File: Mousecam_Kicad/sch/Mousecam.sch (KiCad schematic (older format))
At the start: 16 parts

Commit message: sync
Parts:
- removed U?: TLV7103318DSER, DSE6, symbol Mousecam-rescue:TLV7103318DSER-TLV7103318DSER-Mousecam-rescue
- added U?: TLV7103318DSER, DSE6, symbol TLV7103318DSER:TLV7103318DSER
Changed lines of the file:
@@
 Wire Wire Line
 	8250 5350 8250 5550
-$Comp
-L Mousecam-rescue:TLV7103318DSER-TLV7103318DSER-Mousecam-rescue U?
-U 1 1 607F86D1
-P 2800 1400
-F 0 "U?" H 3450 1787 60  0000 C CNN
-F 1 "TLV7103318DSER" H 3450 1681 60  0000 C CNN
-F 2 "DSE6" H 3450 1650 60  0001 C CNN
-F 3 "" H 2800 1400 60  0000 C CNN
-	1    2800 1400
-	1    0    0    -1
-$EndComp
 $Sheet
 S 9750 5300 1700 1500
@@
 F15 "I2C_SCL" I L 9750 6700 50
 $EndSheet
+$Comp
+L TLV7103318DSER:TLV7103318DSER U?
+U 1 1 608A8B14
+P 2800 1400
+F 0 "U?" H 3450 1787 60  0000 C CNN
+F 1 "TLV7103318DSER" H 3450 1681 60  0000 C CNN
+F 2 "DSE6" H 3450 1650 60  0001 C CNN
+F 3 "" H 2800 1400 60  0000 C CNN
+	1    2800 1400
+	1    0    0    -1
+$EndComp
 $EndSCHEMATC

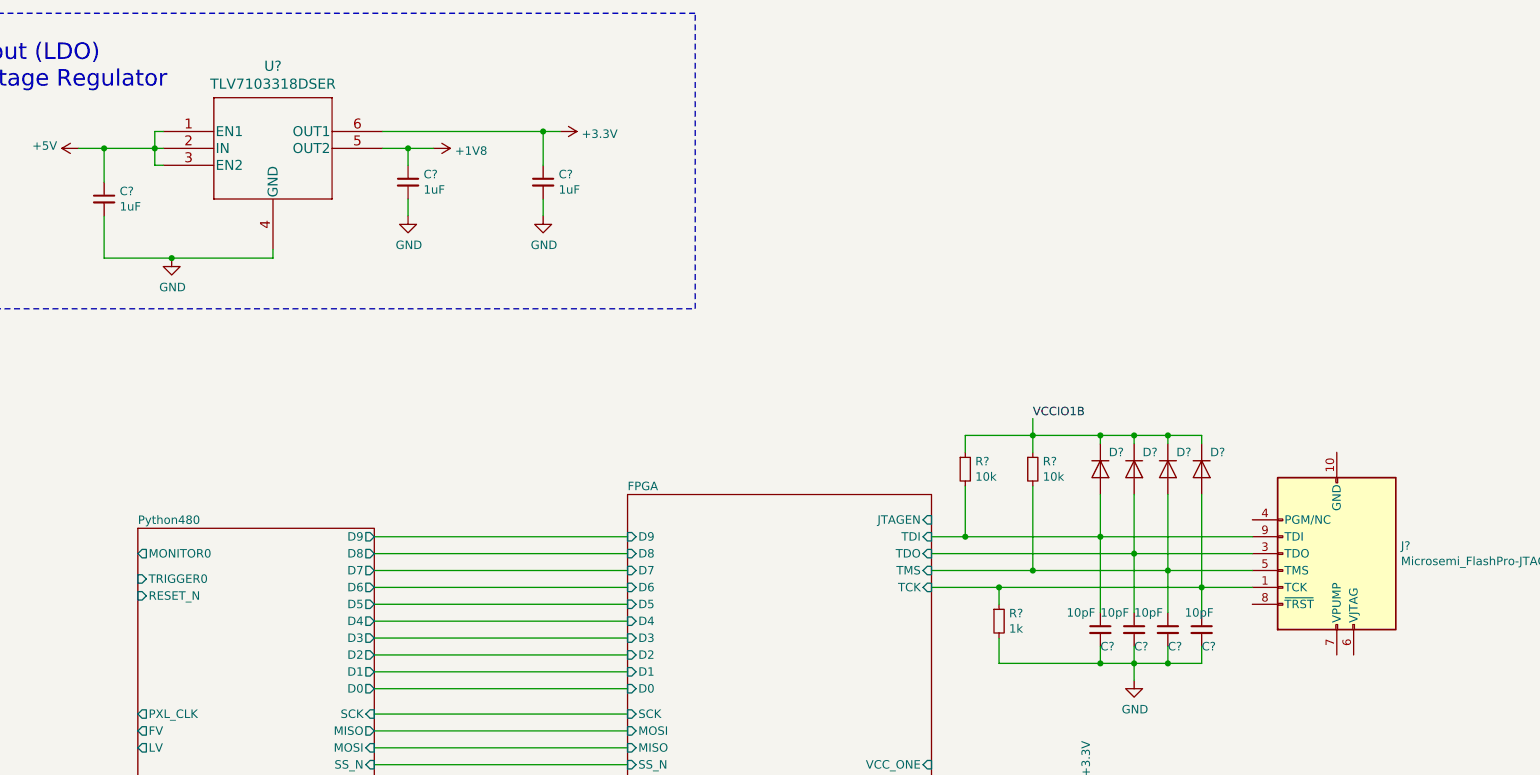
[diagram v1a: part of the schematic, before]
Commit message: updated relative path for libs
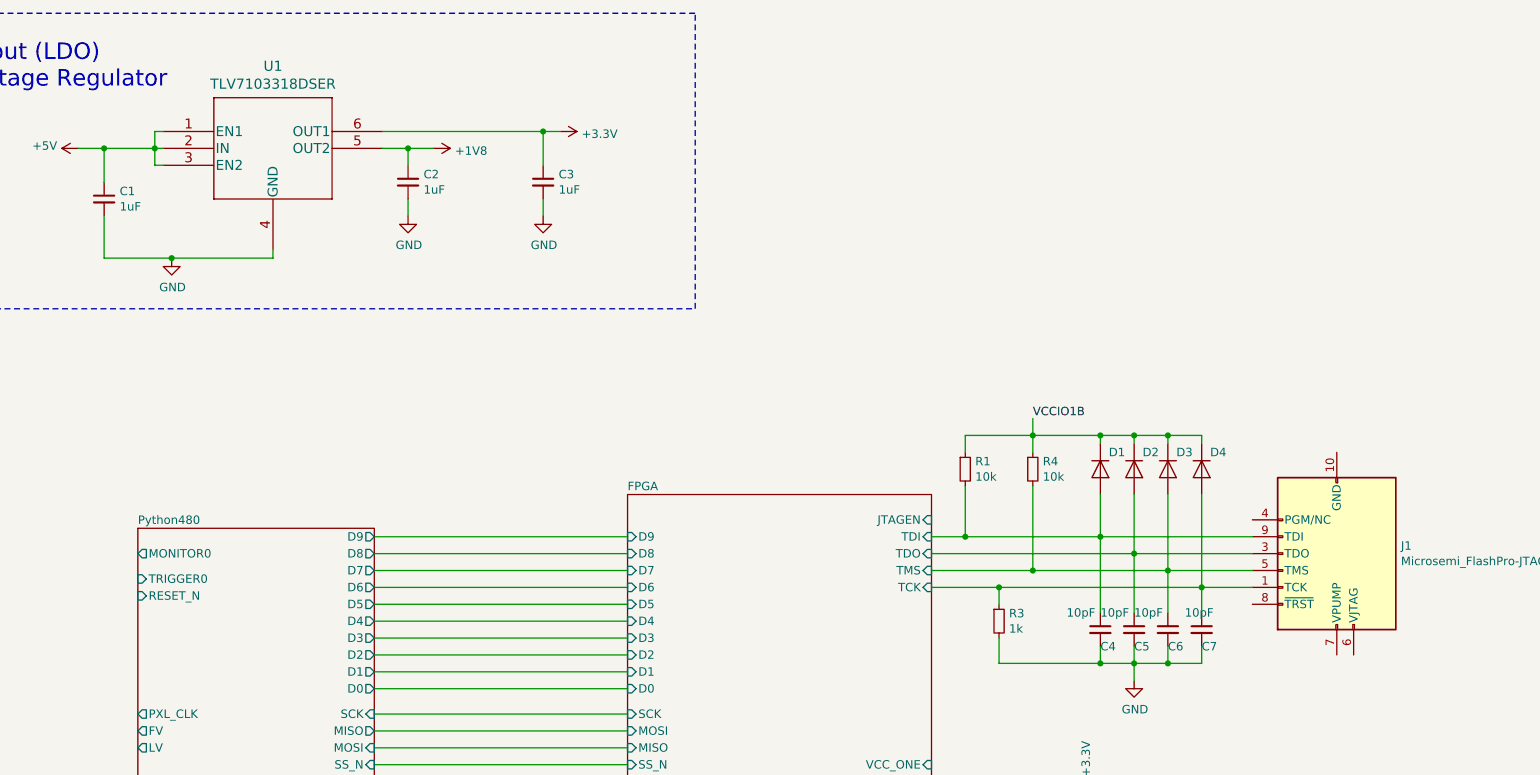
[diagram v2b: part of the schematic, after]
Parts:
- removed U?: TLV7103318DSER, DSE6, symbol TLV7103318DSER:TLV7103318DSER
- added U1: TLV7103318DSER, DSE6, symbol TLV7103318DSER:TLV7103318DSER
- C1, C4, C5, C6, C7: renamed from C?; footprint (none) -> Capacitor_SMD:C_0603_1608Metric_Pad1.05x0.95mm_HandSolder
- C2, C3: renamed from C?; footprint Capacitor_SMD:C_0201_0603Metric -> Capacitor_SMD:C_0603_1608Metric_Pad1.05x0.95mm_HandSolder
- gave numbers to parts that had none: 8
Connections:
- net +1V8: now also U1.5 (OUT2)
- net +3V3: now also U1.6 (OUT1)
- net +5V: now also U1.1 (EN1), U1.2 (IN), U1.3 (EN2)
- net GND: now also U1.4 (GND)
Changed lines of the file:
@@
 	4050 5150 5550 5150
 $Comp
-L Connector:Microsemi_FlashPro-JTAG-10 J?
+L Connector:Microsemi_FlashPro-JTAG-10 J1
 U 1 1 6080A4A0
 P 9750 3900
-F 0 "J?" H 9370 3854 50  0000 R CNN
+F 0 "J1" H 9370 3854 50  0000 R CNN
 F 1 "Microsemi_FlashPro-JTAG-10" H 9370 3945 50  0000 R CNN
 F 2 "" V 9600 4050 50  0001 C CNN
@@
 	7350 3800 7550 3800
 $Comp
-L Device:R_Small R?
+L Device:R_Small R1
 U 1 1 6081BD78
 P 7550 3400
-F 0 "R?" H 7609 3446 50  0000 L CNN
+F 0 "R1" H 7609 3446 50  0000 L CNN
 F 1 "10k" H 7609 3355 50  0000 L CNN
 F 2 "" H 7550 3400 50  0001 C CNN
@@
 	7350 4100 7750 4100
 $Comp
-L Diode:1N4148 D?
+L Diode:1N4148 D2
 U 1 1 60825DCF
 P 8550 3400
-F 0 "D?" V 8450 3450 50  0000 L CNN
+F 0 "D2" V 8450 3450 50  0000 L CNN
 F 1 "1N4148" V 8595 3479 50  0001 L CNN
 F 2 "Diode_THT:D_DO-35_SOD27_P7.62mm_Horizontal" H 8550 3225 50  0001 C CNN
@@
 $EndComp
 $Comp
-L Diode:1N4148 D?
+L Diode:1N4148 D3
 U 1 1 60827201
 P 8750 3400
-F 0 "D?" V 8650 3450 50  0000 L CNN
+F 0 "D3" V 8650 3450 50  0000 L CNN
 F 1 "1N4148" V 8795 3479 50  0001 L CNN
 F 2 "Diode_THT:D_DO-35_SOD27_P7.62mm_Horizontal" H 8750 3225 50  0001 C CNN
@@
 $EndComp
 $Comp
-L Diode:1N4148 D?
+L Diode:1N4148 D4
 U 1 1 608278DD
 P 8950 3400
-F 0 "D?" V 8850 3450 50  0000 L CNN
+F 0 "D4" V 8850 3450 50  0000 L CNN
 F 1 "1N4148" V 8995 3479 50  0001 L CNN
 F 2 "Diode_THT:D_DO-35_SOD27_P7.62mm_Horizontal" H 8950 3225 50  0001 C CNN
@@
 $EndComp
 $Comp
-L Diode:1N4148 D?
+L Diode:1N4148 D1
 U 1 1 6081FF40
 P 8350 3400
-F 0 "D?" V 8250 3450 50  0000 L CNN
+F 0 "D1" V 8250 3450 50  0000 L CNN
 F 1 "1N4148" V 8395 3479 50  0001 L CNN
 F 2 "Diode_THT:D_DO-35_SOD27_P7.62mm_Horizontal" H 8350 3225 50  0001 C CNN
@@
 $EndComp
 $Comp
-L Device:R_Small R?
+L Device:R_Small R4
 U 1 1 608185DA
 P 7950 3400
-F 0 "R?" H 8009 3446 50  0000 L CNN
+F 0 "R4" H 8009 3446 50  0000 L CNN
 F 1 "10k" H 8009 3355 50  0000 L CNN
 F 2 "" H 7950 3400 50  0001 C CNN
@@
 Connection ~ 8950 4100
 $Comp
-L Device:R_Small R?
+L Device:R_Small R3
 U 1 1 60838371
 P 7750 4300
-F 0 "R?" H 7809 4346 50  0000 L CNN
+F 0 "R3" H 7809 4346 50  0000 L CNN
 F 1 "1k" H 7809 4255 50  0000 L CNN
 F 2 "" H 7750 4300 50  0001 C CNN
@@
 Connection ~ 7750 4100
 $Comp
-L Device:C_Small C?
+L Device:C_Small C4
 U 1 1 6083ADA1
 P 8350 4350
-F 0 "C?" H 8350 4250 50  0000 L CNN
+F 0 "C4" H 8350 4250 50  0000 L CNN
 F 1 "10pF" H 8150 4450 50  0000 L CNN
-F 2 "" H 8350 4350 50  0001 C CNN
+F 2 "Capacitor_SMD:C_0603_1608Metric_Pad1.05x0.95mm_HandSolder" H 8350 4350 50  0001 C CNN
 F 3 "~" H 8350 4350 50  0001 C CNN
 	1    8350 4350
@@
 $EndComp
 $Comp
-L Device:C_Small C?
+L Device:C_Small C5
 U 1 1 6083BE5F
 P 8550 4350
-F 0 "C?" H 8550 4250 50  0000 L CNN
+F 0 "C5" H 8550 4250 50  0000 L CNN
 F 1 "10pF" H 8350 4450 50  0000 L CNN
-F 2 "" H 8550 4350 50  0001 C CNN
+F 2 "Capacitor_SMD:C_0603_1608Metric_Pad1.05x0.95mm_HandSolder" H 8550 4350 50  0001 C CNN
 F 3 "~" H 8550 4350 50  0001 C CNN
 	1    8550 4350
@@
 $EndComp
 $Comp
-L Device:C_Small C?
+L Device:C_Small C6
 U 1 1 6083C59F
 P 8750 4350
-F 0 "C?" H 8750 4250 50  0000 L CNN
+F 0 "C6" H 8750 4250 50  0000 L CNN
 F 1 "10pF" H 8550 4450 50  0000 L CNN
-F 2 "" H 8750 4350 50  0001 C CNN
+F 2 "Capacitor_SMD:C_0603_1608Metric_Pad1.05x0.95mm_HandSolder" H 8750 4350 50  0001 C CNN
 F 3 "~" H 8750 4350 50  0001 C CNN
 	1    8750 4350
@@
 $EndComp
 $Comp
-L Device:C_Small C?
+L Device:C_Small C7
 U 1 1 6083CE09
 P 8950 4350
-F 0 "C?" H 8950 4250 50  0000 L CNN
+F 0 "C7" H 8950 4250 50  0000 L CNN
 F 1 "10pF" H 8850 4450 50  0000 L CNN
-F 2 "" H 8950 4350 50  0001 C CNN
+F 2 "Capacitor_SMD:C_0603_1608Metric_Pad1.05x0.95mm_HandSolder" H 8950 4350 50  0001 C CNN
 F 3 "~" H 8950 4350 50  0001 C CNN
 	1    8950 4350
@@
 	8750 4550 8950 4550
 $Comp
-L power:GND #PWR?
+L power:GND #PWR031
 U 1 1 60844BF5
 P 8550 4650
-F 0 "#PWR?" H 8550 4400 50  0001 C CNN
+F 0 "#PWR031" H 8550 4400 50  0001 C CNN
 F 1 "GND" H 8555 4477 50  0000 C CNN
 F 2 "" H 8550 4650 50  0001 C CNN
@@
 P 4250 1700
 AR Path="/607CBDDC/608AC7CF" Ref="C?"  Part="1"
-AR Path="/608AC7CF" Ref="C?"  Part="1"
-F 0 "C?" H 4342 1746 50  0000 L CNN
+AR Path="/608AC7CF" Ref="C2"  Part="1"
+F 0 "C2" H 4342 1746 50  0000 L CNN
 F 1 "1uF" H 4342 1655 50  0000 L CNN
-F 2 "Capacitor_SMD:C_0201_0603Metric" H 4250 1700 50  0001 C CNN
+F 2 "Capacitor_SMD:C_0603_1608Metric_Pad1.05x0.95mm_HandSolder" H 4250 1700 50  0001 C CNN
 F 3 "~" H 4250 1700 50  0001 C CNN
 	1    4250 1700
@@
 P 4250 1900
 AR Path="/607CBDDC/608AC7D5" Ref="#PWR?"  Part="1"
-AR Path="/608AC7D5" Ref="#PWR?"  Part="1"
-F 0 "#PWR?" H 4250 1650 50  0001 C CNN
+AR Path="/608AC7D5" Ref="#PWR026"  Part="1"
+F 0 "#PWR026" H 4250 1650 50  0001 C CNN
 F 1 "GND" H 4255 1727 50  0000 C CNN
 F 2 "" H 4250 1900 50  0001 C CNN
@@
 P 5050 1700
 AR Path="/607CBDDC/608AC7DB" Ref="C?"  Part="1"
-AR Path="/608AC7DB" Ref="C?"  Part="1"
-F 0 "C?" H 5142 1746 50  0000 L CNN
+AR Path="/608AC7DB" Ref="C3"  Part="1"
+F 0 "C3" H 5142 1746 50  0000 L CNN
 F 1 "1uF" H 5142 1655 50  0000 L CNN
-F 2 "Capacitor_SMD:C_0201_0603Metric" H 5050 1700 50  0001 C CNN
+F 2 "Capacitor_SMD:C_0603_1608Metric_Pad1.05x0.95mm_HandSolder" H 5050 1700 50  0001 C CNN
 F 3 "~" H 5050 1700 50  0001 C CNN
 	1    5050 1700
@@
 P 5050 1900
 AR Path="/607CBDDC/608AC7E1" Ref="#PWR?"  Part="1"
-AR Path="/608AC7E1" Ref="#PWR?"  Part="1"
-F 0 "#PWR?" H 5050 1650 50  0001 C CNN
+AR Path="/608AC7E1" Ref="#PWR028"  Part="1"
+F 0 "#PWR028" H 5050 1650 50  0001 C CNN
 F 1 "GND" H 5055 1727 50  0000 C CNN
 F 2 "" H 5050 1900 50  0001 C CNN
@@
 P 4400 1500
 AR Path="/607CBDDC/608AC7E7" Ref="#PWR?"  Part="1"
-AR Path="/608AC7E7" Ref="#PWR?"  Part="1"
-F 0 "#PWR?" H 4400 1350 50  0001 C CNN
+AR Path="/608AC7E7" Ref="#PWR027"  Part="1"
+F 0 "#PWR027" H 4400 1350 50  0001 C CNN
 F 1 "+1V8" V 4415 1628 50  0000 L CNN
 F 2 "" H 4400 1500 50  0001 C CNN
@@
 P 5150 1400
 AR Path="/607CBDDC/608AC7ED" Ref="#PWR?"  Part="1"
-AR Path="/608AC7ED" Ref="#PWR?"  Part="1"
-F 0 "#PWR?" H 5150 1250 50  0001 C CNN
+AR Path="/608AC7ED" Ref="#PWR029"  Part="1"
+F 0 "#PWR029" H 5150 1250 50  0001 C CNN
 F 1 "+3.3V" V 5165 1528 50  0000 L CNN
 F 2 "" H 5150 1400 50  0001 C CNN
@@
 P 2850 2150
 AR Path="/607CBDDC/608AC802" Ref="#PWR?"  Part="1"
-AR Path="/608AC802" Ref="#PWR?"  Part="1"
-F 0 "#PWR?" H 2850 1900 50  0001 C CNN
+AR Path="/608AC802" Ref="#PWR025"  Part="1"
+F 0 "#PWR025" H 2850 1900 50  0001 C CNN
 F 1 "GND" H 2855 1977 50  0000 C CNN
 F 2 "" H 2850 2150 50  0001 C CNN
@@
 P 2450 1800
 AR Path="/607CBDDC/608AC808" Ref="C?"  Part="1"
-AR Path="/608AC808" Ref="C?"  Part="1"
-F 0 "C?" H 2542 1846 50  0000 L CNN
+AR Path="/608AC808" Ref="C1"  Part="1"
+F 0 "C1" H 2542 1846 50  0000 L CNN
 F 1 "1uF" H 2542 1755 50  0000 L CNN
-F 2 "" H 2450 1800 50  0001 C CNN
+F 2 "Capacitor_SMD:C_0603_1608Metric_Pad1.05x0.95mm_HandSolder" H 2450 1800 50  0001 C CNN
 F 3 "~" H 2450 1800 50  0001 C CNN
 	1    2450 1800
@@
 P 2300 1500
 AR Path="/607CBDDC/608AC80E" Ref="#PWR?"  Part="1"
-AR Path="/608AC80E" Ref="#PWR?"  Part="1"
-F 0 "#PWR?" H 2300 1350 50  0001 C CNN
+AR Path="/608AC80E" Ref="#PWR024"  Part="1"
+F 0 "#PWR024" H 2300 1350 50  0001 C CNN
 F 1 "+5V" V 2315 1628 50  0000 L CNN
 F 2 "" H 2300 1500 50  0001 C CNN
@@
 P 8250 5350
 AR Path="/607CBDDC/60919579" Ref="#PWR?"  Part="1"
-AR Path="/60919579" Ref="#PWR?"  Part="1"
-F 0 "#PWR?" H 8250 5200 50  0001 C CNN
+AR Path="/60919579" Ref="#PWR030"  Part="1"
+F 0 "#PWR030" H 8250 5200 50  0001 C CNN
 F 1 "+3.3V" V 8265 5478 50  0000 L CNN
 F 2 "" H 8250 5350 50  0001 C CNN
@@
 $EndSheet
 $Comp
-L TLV7103318DSER:TLV7103318DSER U?
-U 1 1 608A8B14
+L TLV7103318DSER:TLV7103318DSER U1
+U 1 1 608B2FA3
 P 2800 1400
-F 0 "U?" H 3450 1787 60  0000 C CNN
+F 0 "U1" H 3450 1787 60  0000 C CNN
 F 1 "TLV7103318DSER" H 3450 1681 60  0000 C CNN
 F 2 "DSE6" H 3450 1650 60  0001 C CNN
